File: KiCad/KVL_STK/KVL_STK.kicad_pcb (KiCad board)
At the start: 2 copper layers, 222.4 x 77.5 mm, 167 parts, among them J1 AudioJack2_Ground, J2 Conn_01x04, J3 AudioJack2_Ground, J4 Conn_01x08, SW1 SW_MEC_5G, SW10 SW_MEC_5G, SW14 SW_MEC_5G, SW15 SW_MEC_5G, SW16 SW_MEC_5G, SW17 SW_MEC_5G, SW18 SW_MEC_5G, SW19 SW_MEC_5G, SW2 SW_MEC_5G, SW20 SW_MEC_5G, SW21 SW_MEC_5G, SW22 SW_MEC_5G, SW23 SW_MEC_5G, SW27 SW_MEC_5G, SW28 SW_MEC_5G, SW29 SW_MEC_5G, SW3 SW_MEC_5G, SW30 SW_MEC_5G, SW31 SW_MEC_5G, SW32 SW_MEC_5G, SW33 SW_MEC_5G, SW34 SW_MEC_5G, SW35 SW_MEC_5G, SW36 SW_MEC_5G, SW4 SW_MEC_5G, SW41 SW_MEC_5G, SW42 SW_MEC_5G, SW44 SW_MEC_5G, SW46 SW_MEC_5G, SW47 SW_MEC_5G, SW48 SW_MEC_5G, SW49 SW_MEC_5G, SW5 SW_MEC_5G, SW6 SW_MEC_5G, SW7 SW_MEC_5G, SW8 SW_MEC_5G, SW9 SW_MEC_5G, U1 74HC164, U2 74HC165, U3 74HC165, U5 ADAU1761BCPZ, U6 MIC2005A-1YM5-TR

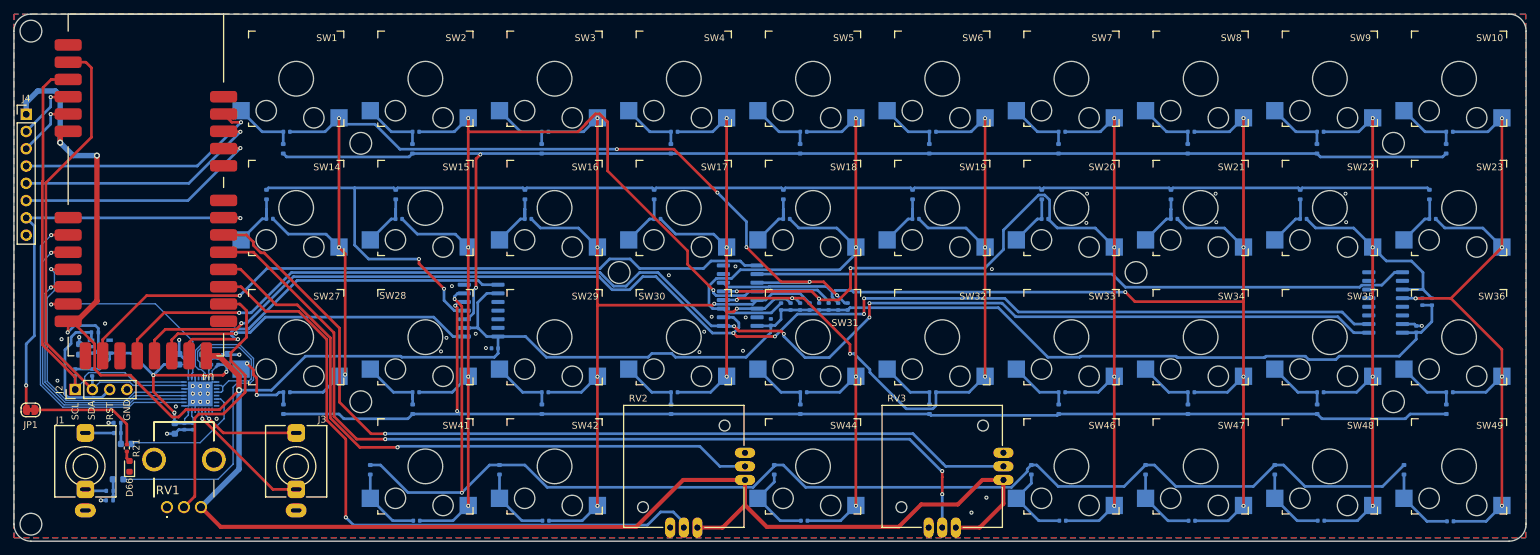
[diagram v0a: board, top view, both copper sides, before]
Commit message: Added 30 RGB LEDs.
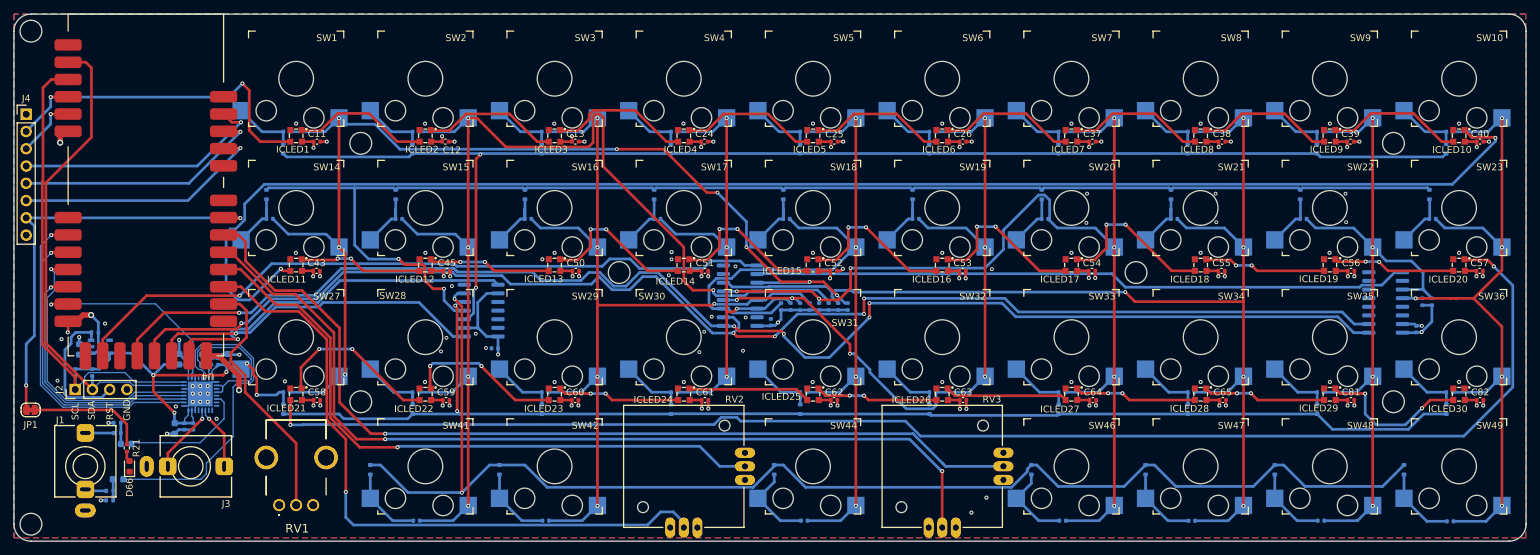
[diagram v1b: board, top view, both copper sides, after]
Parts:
- added C11: 100nF, Capacitor_SMD:C_0402_1005Metric, F.Cu at (103.0, 109.2)
- added C12: 100nF, Capacitor_SMD:C_0402_1005Metric, F.Cu at (122.0, 109.2)
- added C13: 100nF, Capacitor_SMD:C_0402_1005Metric, F.Cu at (141.1, 109.2)
- added C24: 100nF, Capacitor_SMD:C_0402_1005Metric, F.Cu at (160.0, 109.2)
- added C25: 100nF, Capacitor_SMD:C_0402_1005Metric, F.Cu at (179.1, 109.2)
- added C26: 100nF, Capacitor_SMD:C_0402_1005Metric, F.Cu at (198.0, 109.2)
- added C37: 100nF, Capacitor_SMD:C_0402_1005Metric, F.Cu at (217.1, 109.2)
- added C38: 100nF, Capacitor_SMD:C_0402_1005Metric, F.Cu at (236.1, 109.2)
- added C39: 100nF, Capacitor_SMD:C_0402_1005Metric, F.Cu at (255.0, 109.2)
- added C40: 100nF, Capacitor_SMD:C_0402_1005Metric, F.Cu at (274.1, 109.2)
- added C43: 100nF, Capacitor_SMD:C_0402_1005Metric, F.Cu at (103.0, 128.2)
- added C45: 100nF, Capacitor_SMD:C_0402_1005Metric, F.Cu at (122.2, 128.2)
- added C50: 100nF, Capacitor_SMD:C_0402_1005Metric, F.Cu at (141.1, 128.2)
- added C51: 100nF, Capacitor_SMD:C_0402_1005Metric, F.Cu at (160.1, 128.2)
- added C52: 100nF, Capacitor_SMD:C_0402_1005Metric, F.Cu at (179.0, 128.2)
- added C53: 100nF, Capacitor_SMD:C_0402_1005Metric, F.Cu at (198.0, 128.2)
- added C54: 100nF, Capacitor_SMD:C_0402_1005Metric, F.Cu at (217.0, 128.2)
- added C55: 100nF, Capacitor_SMD:C_0402_1005Metric, F.Cu at (236.1, 128.2)
- added C56: 100nF, Capacitor_SMD:C_0402_1005Metric, F.Cu at (255.1, 128.2)
- added C57: 100nF, Capacitor_SMD:C_0402_1005Metric, F.Cu at (274.0, 128.2)
- added C58: 100nF, Capacitor_SMD:C_0402_1005Metric, F.Cu at (103.0, 147.2)
- added C59: 100nF, Capacitor_SMD:C_0402_1005Metric, F.Cu at (122.0, 147.2)
- added C60: 100nF, Capacitor_SMD:C_0402_1005Metric, F.Cu at (141.0, 147.2)
- added C61: 100nF, Capacitor_SMD:C_0402_1005Metric, F.Cu at (160.1, 147.2)
- added C62: 100nF, Capacitor_SMD:C_0402_1005Metric, F.Cu at (179.1, 147.2)
- added C63: 100nF, Capacitor_SMD:C_0402_1005Metric, F.Cu at (198.1, 147.2)
- added C64: 100nF, Capacitor_SMD:C_0402_1005Metric, F.Cu at (217.2, 147.2)
- added C65: 100nF, Capacitor_SMD:C_0402_1005Metric, F.Cu at (236.2, 147.2)
- added C81: 100nF, Capacitor_SMD:C_0402_1005Metric, F.Cu at (255.1, 147.2)
- added C82: 100nF, Capacitor_SMD:C_0402_1005Metric, F.Cu at (274.1, 147.2)
- added ICLED1: ~, My_Parts:1312020030000, F.Cu at (100.0, 108.4)
- added ICLED10: ~, My_Parts:1312020030000, F.Cu at (271.0, 108.4)
- added ICLED11: ~, My_Parts:1312020030000, F.Cu at (100.0, 127.4)
- added ICLED12: ~, My_Parts:1312020030000, F.Cu at (119.0, 127.4)
- added ICLED13: ~, My_Parts:1312020030000, F.Cu at (138.0, 127.4)
- added ICLED14: ~, My_Parts:1312020030000, F.Cu at (157.0, 127.4)
- added ICLED15: ~, My_Parts:1312020030000, F.Cu at (176.0, 127.4)
- added ICLED16: ~, My_Parts:1312020030000, F.Cu at (195.0, 127.4)
- added ICLED17: ~, My_Parts:1312020030000, F.Cu at (214.0, 127.4)
- added ICLED18: ~, My_Parts:1312020030000, F.Cu at (233.0, 127.4)
- added ICLED19: ~, My_Parts:1312020030000, F.Cu at (252.0, 127.4)
- added ICLED2: ~, My_Parts:1312020030000, F.Cu at (119.0, 108.4)
- added ICLED20: ~, My_Parts:1312020030000, F.Cu at (271.0, 127.4)
- added ICLED21: ~, My_Parts:1312020030000, F.Cu at (100.0, 146.4)
- added ICLED22: ~, My_Parts:1312020030000, F.Cu at (119.0, 146.4)
- added ICLED23: ~, My_Parts:1312020030000, F.Cu at (138.0, 146.4)
- added ICLED24: ~, My_Parts:1312020030000, F.Cu at (157.0, 146.4)
- added ICLED25: ~, My_Parts:1312020030000, F.Cu at (176.0, 146.4)
- added ICLED26: ~, My_Parts:1312020030000, F.Cu at (195.0, 146.4)
- added ICLED27: ~, My_Parts:1312020030000, F.Cu at (214.0, 146.4)
- added ICLED28: ~, My_Parts:1312020030000, F.Cu at (233.0, 146.4)
- added ICLED29: ~, My_Parts:1312020030000, F.Cu at (252.0, 146.4)
- added ICLED3: ~, My_Parts:1312020030000, F.Cu at (138.0, 108.4)
- added ICLED30: ~, My_Parts:1312020030000, F.Cu at (271.0, 146.4)
- added ICLED4: ~, My_Parts:1312020030000, F.Cu at (157.0, 108.4)
- added ICLED5: ~, My_Parts:1312020030000, F.Cu at (176.0, 108.4)
- added ICLED6: ~, My_Parts:1312020030000, F.Cu at (195.0, 108.4)
- added ICLED7: ~, My_Parts:1312020030000, F.Cu at (214.0, 108.4)
- added ICLED8: ~, My_Parts:1312020030000, F.Cu at (233.0, 108.4)
- added ICLED9: ~, My_Parts:1312020030000, F.Cu at (252.0, 108.4)
- moved RV1 16.5 mm to (100.0, 162.7)
- moved J3 15.5 mm to (84.5, 157.0), turned to -90 degrees
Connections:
- net /ICs/PA15 renamed PA15
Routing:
- net VCC: track 489.5 -> 143.4 mm, vias 4 -> 37
- net Net-(ICLED10-DOUT): track 0.00 -> 219.5 mm, vias 0 -> 2
- net Net-(ICLED20-DOUT): track 0.00 -> 211.8 mm, vias 0 -> 2
- net PA15: track 9.11 -> 52.2 mm, vias 1 -> 2
- net GND: track 34.5 -> 60.9 mm, vias 42 -> 104
- net Net-(ICLED21-DOUT): track 0.00 -> 24.8 mm, vias 0 -> 2
- net Net-(ICLED17-DOUT): track 0.00 -> 24.4 mm, vias 0 -> 2
- net Net-(ICLED16-DOUT): track 0.00 -> 24.2 mm, vias 0 -> 2
- net Net-(ICLED15-DOUT): track 0.00 -> 23.8 mm, vias 0 -> 2
- net Net-(ICLED14-DOUT): track 0.00 -> 23.4 mm, vias 0 -> 2
- net Net-(ICLED13-DOUT): track 0.00 -> 23.4 mm, vias 0 -> 2
- net Net-(ICLED22-DOUT): track 0.00 -> 23.3 mm, vias 0 -> 2
- net Net-(ICLED29-DOUT): track 0.00 -> 22.8 mm, vias 0 -> 2
- net Net-(ICLED3-DOUT): track 0.00 -> 20.9 mm
- net Net-(ICLED1-DOUT): track 0.00 -> 20.2 mm
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- added copper zone on In1.Cu, net GND
- added copper zone on In2.Cu, net VCC
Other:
- copper layers 2 -> 4

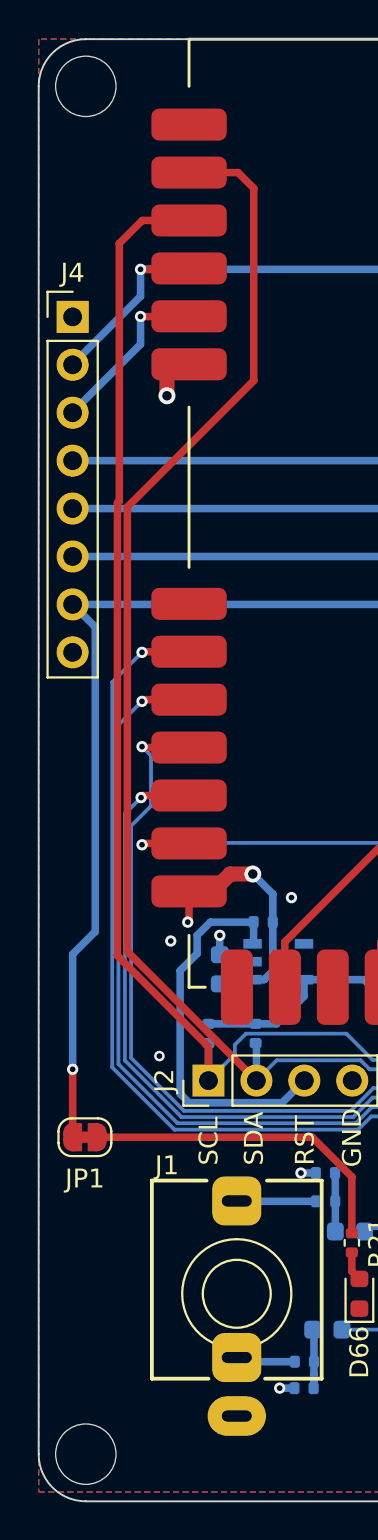
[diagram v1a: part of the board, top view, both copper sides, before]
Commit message: Adjustment of screw hole position.
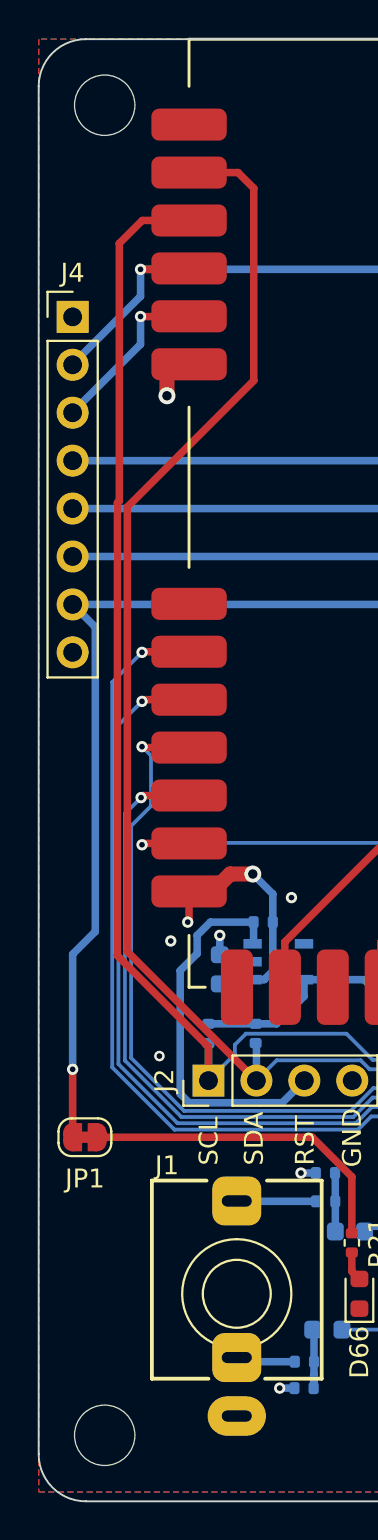
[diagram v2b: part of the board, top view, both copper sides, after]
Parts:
- moved MH7 1.41 mm to (62.0, 94.0)
- moved MH8 1.41 mm to (62.0, 164.5)
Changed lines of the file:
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@@
 	(footprint "MountingHole:MountingHole_3.2mm_M3"
 		(layer "F.Cu")
-		(at 61 93)
+		(at 62 94)
 		(descr "Mounting Hole 3.2mm, no annular, M3")
 		(tags "mounting hole 3.2mm no annular m3")
@@
 	(footprint "MountingHole:MountingHole_3.2mm_M3"
 		(layer "F.Cu")
-		(at 61 165.5)
+		(at 62 164.5)
 		(descr "Mounting Hole 3.2mm, no annular, M3")
 		(tags "mounting hole 3.2mm no annular m3")
@@
 	)
 	(dimension
-		(type aligned)
+		(type orthogonal)
 		(layer "Cmts.User")
 		(pts
-			(xy 109.5 90.6) (xy 61 90.6)
+			(xy 109.5 109.5) (xy 62 94)
 		)
-		(height 2.2)
-		(gr_text "48.50"
-			(at 85.25 87.25 0)
+		(height -53.2)
+		(orientation 1)
+		(gr_text "15.50"
+			(at 55.15 101.75 90)
 			(layer "Cmts.User")
 			(effects
@@
 	)
 	(dimension
-		(type aligned)
+		(type orthogonal)
 		(layer "Cmts.User")
 		(pts
-			(xy 58.5 90.5) (xy 61 90.5)
+			(xy 147.475 128.475) (xy 223.475 128.525)
 		)
-		(height -2.1)
-		(gr_text "2.50"
-			(at 59.75 87.25 0)
+		(height -40.075)
+		(orientation 0)
+		(gr_text "76.00"
+			(at 185.475 87.25 0)
 			(layer "Cmts.User")
 			(effects
@@
 		(layer "Cmts.User")
 		(pts
-			(xy 61 165.5) (xy 56.3 147.525)
+			(xy 147.475 128.475) (xy 109.475 109.525)
 		)
-		(height -4.7)
-		(orientation 1)
-		(gr_text "17.9750"
-			(at 55.15 156.5125 90)
+		(height -40.075)
+		(orientation 0)
+		(gr_text "38.00"
+			(at 128.475 87.25 0)
 			(layer "Cmts.User")
 			(effects
@@
 			(units 3)
 			(units_format 0)
-			(precision 4)
+			(precision 2)
 		)
 		(style
@@
 		(layer "Cmts.User")
 		(pts
-			(xy 61 165.5) (xy 58.7 168)
+			(xy 62 94) (xy 109.5 109.5)
 		)
-		(height -4.7)
-		(orientation 1)
-		(gr_text "2.50"
-			(at 55.15 166.75 90)
+		(height -5.6)
+		(orientation 0)
+		(gr_text "47.50"
+			(at 85.75 87.25 0)
 			(layer "Cmts.User")
 			(effects
@@
 		(layer "Cmts.User")
 		(pts
-			(xy 147.475 128.475) (xy 223.475 128.525)
+			(xy 61 168) (xy 61 90.5)
 		)
-		(height -40.075)
-		(orientation 0)
-		(gr_text "76.00"
-			(at 185.475 87.25 0)
+		(height -7.95)
+		(orientation 1)
+		(gr_text "77.50"
+			(at 51.9 129.25 90)
 			(layer "Cmts.User")
 			(effects
@@
 		(layer "Cmts.User")
 		(pts
-			(xy 109.525 109.475) (xy 61 93)
+			(xy 62 94) (xy 61.7 90.5)
 		)
-		(height -53.225)
+		(height -5.7)
 		(orientation 1)
-		(gr_text "16.4750"
-			(at 55.15 101.2375 90)
+		(gr_text "3.5"
+			(at 55.15 92.25 90)
 			(layer "Cmts.User")
 			(effects
@@
 			(units 3)
 			(units_format 0)
-			(precision 4)
+			(precision 1)
 		)
 		(style
@@
 		(layer "Cmts.User")
 		(pts
-			(xy 61 168) (xy 61 90.5)
+			(xy 280.85 128.51) (xy 223.5 128.5)
 		)
-		(height -7.95)
-		(orientation 1)
-		(gr_text "77.50"
-			(at 51.9 129.25 90)
+		(height -40.11)
+		(orientation 0)
+		(gr_text "57.35"
+			(at 252.175 87.25 0)
 			(layer "Cmts.User")
 			(effects
@@
 		(layer "Cmts.User")
 		(pts
-			(xy 58.5 93) (xy 280.85 93)
+			(xy 62 94) (xy 58.5 93.65)
 		)
-		(height -8.05)
+		(height -5.6)
 		(orientation 0)
-		(gr_text "222.35"
-			(at 169.675 83.8 0)
+		(gr_text "3.5"
+			(at 60.25 87.25 0)
 			(layer "Cmts.User")
 			(effects
@@
 			(units 3)
 			(units_format 0)
-			(precision 2)
+			(precision 1)
 		)
 		(style
@@
 		(layer "Cmts.User")
 		(pts
-			(xy 61 93) (xy 58.5 90.5)
+			(xy 62 164.5) (xy 147.48 128.5)
 		)
-		(height -4.7)
+		(height -5.7)
 		(orientation 1)
-		(gr_text "2.50"
-			(at 55.15 91.75 90)
+		(gr_text "36.00"
+			(at 55.15 146.5 90)
 			(layer "Cmts.User")
 			(effects
@@
 		(layer "Cmts.User")
 		(pts
-			(xy 223.525 128.475) (xy 109.475 109.475)
+			(xy 62 164.5) (xy 61 168)
 		)
-		(height -167.225)
+		(height -5.7)
 		(orientation 1)
-		(gr_text "19.00"
-			(at 55.15 118.975 90)
+		(gr_text "3.5"
+			(at 55.15 166.25 90)
 			(layer "Cmts.User")
 			(effects
@@
 			(units 3)
 			(units_format 0)
-			(precision 2)
+			(precision 1)
 		)
 		(style
@@
 		(layer "Cmts.User")
 		(pts
-			(xy 109.475 109.525) (xy 147.525 128.525)
+			(xy 58.5 93) (xy 280.85 93)
 		)
-		(height -21.125)
+		(height -8.05)
 		(orientation 0)
-		(gr_text "38.05"
-			(at 128.5 87.25 0)
+		(gr_text "222.35"
+			(at 169.675 83.8 0)
 			(layer "Cmts.User")
 			(effects
@@
 		(layer "Cmts.User")
 		(pts
-			(xy 223.475 128.525) (xy 280.85 90.5)
+			(xy 147.5 128.5) (xy 109.5 109.5)
 		)
-		(height -40.125)
-		(orientation 0)
-		(gr_text "57.3750"
-			(at 252.1625 87.25 0)
+		(height -91.2)
+		(orientation 1)
+		(gr_text "19.00"
+			(at 55.15 119 90)
 			(layer "Cmts.User")
 			(effects
@@
 			(units 3)
 			(units_format 0)
-			(precision 4)
+			(precision 2)
 		)
 		(style

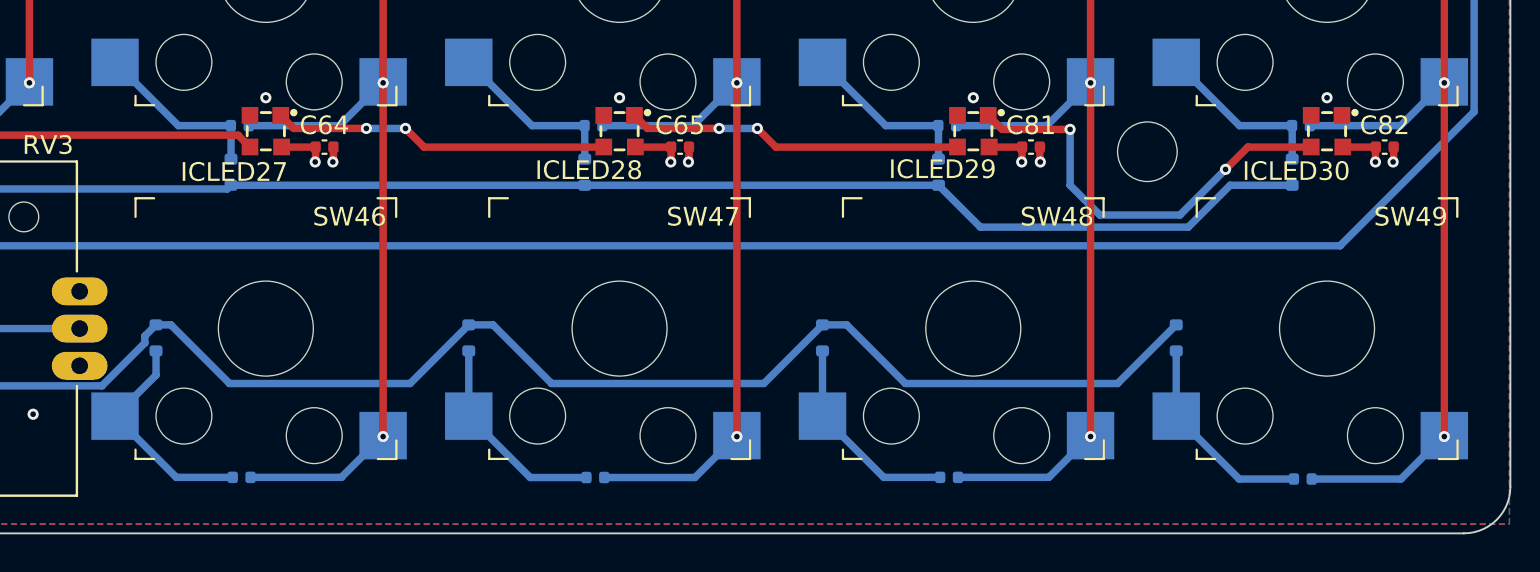
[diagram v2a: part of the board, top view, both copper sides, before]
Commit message: Added four LEDs.
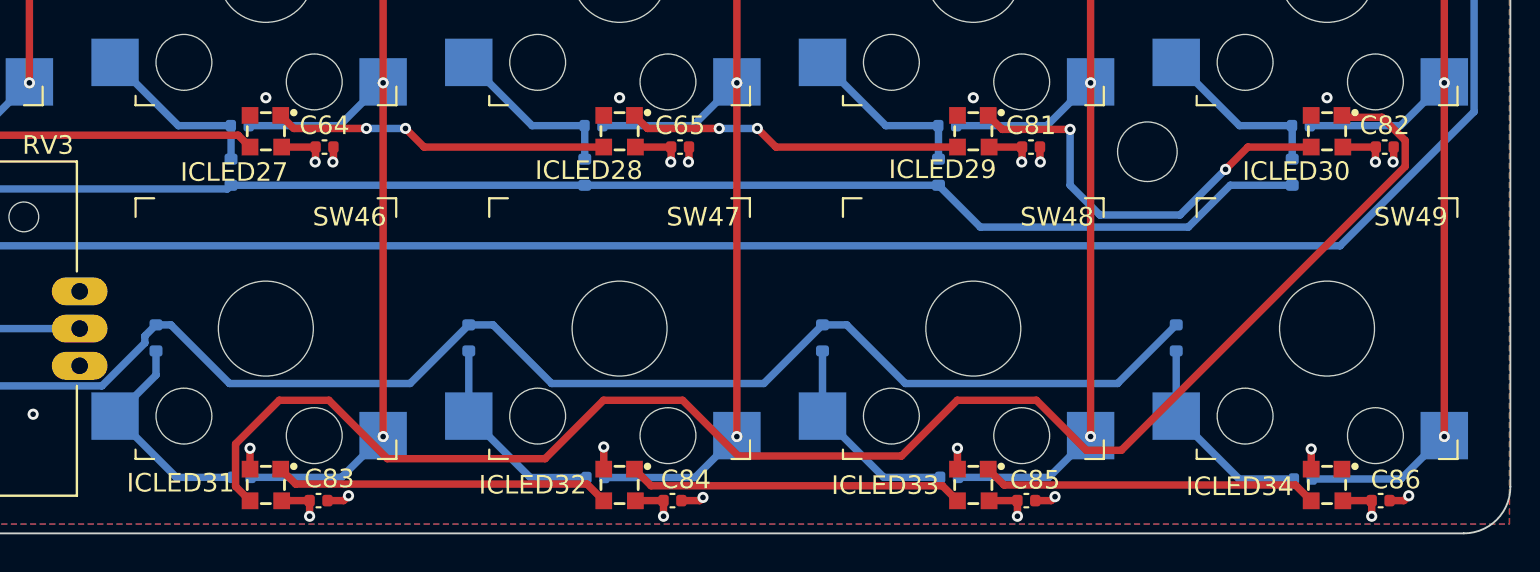
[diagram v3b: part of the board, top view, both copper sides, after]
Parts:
- added C83: 100nF, Capacitor_SMD:C_0402_1005Metric, F.Cu at (216.8, 166.2)
- added C84: 100nF, Capacitor_SMD:C_0402_1005Metric, F.Cu at (235.8, 166.2)
- added C85: 100nF, Capacitor_SMD:C_0402_1005Metric, F.Cu at (254.8, 166.2)
- added C86: 100nF, Capacitor_SMD:C_0402_1005Metric, F.Cu at (273.9, 166.2)
- added ICLED31: ~, My_Parts:1312020030000, F.Cu at (214.0, 165.4)
- added ICLED32: ~, My_Parts:1312020030000, F.Cu at (233.0, 165.4)
- added ICLED33: ~, My_Parts:1312020030000, F.Cu at (252.0, 165.4)
- added ICLED34: ~, My_Parts:1312020030000, F.Cu at (271.0, 165.4)
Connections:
- ICLED30 pad 1: unconnected-(ICLED30-DOUT-Pad1) -> Net-(ICLED30-DOUT)
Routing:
- net Net-(ICLED30-DOUT): track 0.00 -> 85.0 mm
- net Net-(ICLED32-DOUT): track 0.00 -> 18.1 mm
- net Net-(ICLED31-DOUT): track 0.00 -> 18.1 mm
- net Net-(ICLED33-DOUT): track 0.00 -> 18.1 mm
- net VCC: track 143.4 -> 152.9 mm, vias 37 -> 41
- net GND: track 60.9 -> 70.2 mm, vias 104 -> 112
